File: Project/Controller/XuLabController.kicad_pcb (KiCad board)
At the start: 4 copper layers, 115 x 123 mm, 75 parts, among them J1 SWD Connector, J10 Servo, J11 Servo, J12 Thruster, J13 USB_B_Micro, J14 CAN, J15 I2C, J16 UART, J2 Conn_01x04, J3 1986660-2, J4 Servo, J5 Servo, J6 Servo, J7 Servo, J8 Servo, J9 Servo, Q2 PMOS, SW1 SW_Push, SW2 SW_SPDT, SW3 SW_SPDT, U1 STM32F446RCTx, U2 BMI088, U3 MMC5983MA, U4 AP63203WU, U5 TVS0500DRV, Y1 25 MHz

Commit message: Add initial layout
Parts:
- removed FL1: 0805USB-502MLC, Inductor_SMD:L_CommonModeChoke_Coilcraft_0805USB
- removed L1: 3.9uH, Inductor_SMD:L_Pulse_PA4334
- removed Q2: PMOS, XuLab:SOP-Advance-8
- removed TP2, TP3, TP4, TP5: TestPoint, TestPoint:TestPoint_Plated_Hole_D2.0mm
- added C26: 10uF, Capacitor_SMD:C_1206_3216Metric, F.Cu at (166.0, 86.0)
- added C27: 100nF, Capacitor_SMD:C_0603_1608Metric, B.Cu at (123.5, 64.5)
- added C28: 100nF, Capacitor_SMD:C_0603_1608Metric, B.Cu at (166.5, 64.5)
- added C29: 100nF, Capacitor_SMD:C_0603_1608Metric, B.Cu at (114.0, 70.0)
- added C30: 100nF, Capacitor_SMD:C_0603_1608Metric, B.Cu at (177.0, 70.0)
- added C31: 100nF, Capacitor_SMD:C_0603_1608Metric, B.Cu at (138.0, 64.5)
- added C32: 100nF, Capacitor_SMD:C_0603_1608Metric, B.Cu at (153.0, 64.5)
- added H1: MH, MountingHole:MountingHole_2.7mm_M2.5_Pad_Via, F.Cu at (121.0, 78.0)
- added H2: MH, MountingHole:MountingHole_2.7mm_M2.5_Pad_Via, F.Cu at (170.0, 78.0)
- added H3: MH, MountingHole:MountingHole_2.7mm_M2.5_Pad_Via, F.Cu at (121.0, 136.0)
- added H4: MH, MountingHole:MountingHole_2.7mm_M2.5_Pad_Via, F.Cu at (170.0, 136.0)
- added J17: UART2, Connector_JST:JST_GH_SM04B-GHS-TB_1x04-1MP_P1.25mm_Horizontal, F.Cu at (179.0, 70.0)
- added J18: SPI1, Connector_JST:JST_GH_SM06B-GHS-TB_1x06-1MP_P1.25mm_Horizontal, F.Cu at (138.0, 62.5)
- added J19: SPI2, Connector_JST:JST_GH_SM06B-GHS-TB_1x06-1MP_P1.25mm_Horizontal, F.Cu at (153.0, 62.5)
- added J20: Interrupt, Connector_Molex:Molex_KK-254_AE-6410-02A_1x02_P2.54mm_Vertical, F.Cu at (112.0, 93.5)
- added J21: Interrupt, Connector_Molex:Molex_KK-254_AE-6410-02A_1x02_P2.54mm_Vertical, F.Cu at (112.0, 86.5)
- added J22: Interrupt, Connector_Molex:Molex_KK-254_AE-6410-02A_1x02_P2.54mm_Vertical, F.Cu at (112.0, 79.5)
- added R12: 5k1, Resistor_SMD:R_0603_1608Metric, F.Cu at (154.0, 130.0)
- added R13: 5k1, Resistor_SMD:R_0603_1608Metric, F.Cu at (164.0, 130.0)
- added R14: 82k, Resistor_SMD:R_0603_1608Metric, B.Cu at (155.5, 101.5)
- added U6: USBLC6-2SC6, Package_TO_SOT_SMD:SOT-23-6, F.Cu at (159.0, 127.0)
- added U7: BMI088, Package_LGA:Bosch_LGA-16_4.5x3mm_P0.5mm_LayoutBorder7x1y_ClockwisePinNumbering, F.Cu at (154.0, 86.0)
- added U8: MMC5983MA, XuLab:MMC5983MA_MEM, F.Cu at (162.5, 86.0)
- added U9: MCP9700Ax-ETT, Package_TO_SOT_SMD:SOT-23, B.Cu at (129.0, 105.0)
- C1: value 4.7uF -> 1uF
- C10, C14, C22: footprint Capacitor_SMD:C_0402_1005Metric -> Capacitor_SMD:C_0603_1608Metric; moved to B.Cu
- C11, C12: value 22pF -> 100nF; footprint Capacitor_SMD:C_0402_1005Metric -> Capacitor_SMD:C_0603_1608Metric; moved to B.Cu
- C13: value 100nF -> 1uF; footprint Capacitor_SMD:C_0402_1005Metric -> Capacitor_SMD:C_0603_1608Metric; moved to B.Cu
- C15: value 1uF -> 100nF
- C16: value 10uF -> 27pF; footprint Capacitor_SMD:C_1206_3216Metric -> Capacitor_SMD:C_0603_1608Metric
- C17: value 100nF -> 27pF; footprint Capacitor_SMD:C_0402_1005Metric -> Capacitor_SMD:C_0603_1608Metric
- C18: value 100uF -> 100nF; footprint Capacitor_SMD:C_1210_3225Metric -> Capacitor_SMD:C_0603_1608Metric
- C19: value 10uF -> 2.2uF; footprint Capacitor_SMD:C_1206_3216Metric -> Capacitor_SMD:C_0603_1608Metric
- C2: value 100nF -> 10uF; footprint Capacitor_SMD:C_0402_1005Metric -> Capacitor_SMD:C_1206_3216Metric
- C20: value 1uF -> 100nF; moved to B.Cu
- C21: value 10uF -> 100nF; footprint Capacitor_SMD:C_1206_3216Metric -> Capacitor_SMD:C_0603_1608Metric; moved to B.Cu
- C23, C24: value 22uF -> 100nF; moved to B.Cu
- C25, C3, C6: value 100nF -> 1uF; footprint Capacitor_SMD:C_0402_1005Metric -> Capacitor_SMD:C_0603_1608Metric
- C4: value 100nF -> 470pF; footprint Capacitor_SMD:C_0402_1005Metric -> Capacitor_SMD:C_0603_1608Metric
- C5: value 100nF -> 2.2uF; footprint Capacitor_SMD:C_0402_1005Metric -> Capacitor_Tantalum_SMD:CP_EIA-3216-18_Kemet-A
- C7: value 1uF -> 4.7uF
- C8: footprint Capacitor_SMD:C_0402_1005Metric -> Capacitor_SMD:C_0603_1608Metric
- C9: value 2.2uF -> 100nF; moved to B.Cu
- D1: value LED -> 5V; footprint LED_SMD:LED_0603_1608Metric -> Diode_SMD:D_PowerDI-123
- D2: value RCLAMP0582B -> Red; footprint Package_TO_SOT_SMD:SOT-416 -> LED_SMD:LED_0603_1608Metric
- D3: value 12V -> Amber; footprint Diode_SMD:D_SOD-123 -> LED_SMD:LED_0603_1608Metric
- D4: value 7.5V -> Green; footprint Diode_SMD:D_SMB -> LED_SMD:LED_0603_1608Metric
- D5: value 3.3V -> Blue; footprint Diode_SMD:D_MicroSMP_KA -> LED_SMD:LED_0603_1608Metric
- FB1: moved to F.Cu
- J1: value SWD Connector -> Power; footprint Connector_IDC:IDC-Header_2x05_P2.54mm_Vertical -> Connector_JST:JST_GH_SM02B-GHS-TB_1x02-1MP_P1.25mm_Horizontal
- J10, J11, J5, J6, J7, J8, J9: footprint TerminalBlock_Phoenix:TerminalBlock_Phoenix_MKDS-1,5-3-5.08_1x03_P5.08mm_Horizontal -> Connector_JST:JST_VH_B2P-VH_1x02_P3.96mm_Vertical
- J12: value Thruster -> Servo; footprint Connector_JST:JST_VH_B3P-VH_1x03_P3.96mm_Vertical -> Connector_JST:JST_VH_B2P-VH_1x02_P3.96mm_Vertical
- J13: value USB_B_Micro -> Thruster; footprint Connector_USB:USB_Micro-B_Molex_47346-0001 -> Connector_JST:JST_VH_B2P-VH_1x02_P3.96mm_Vertical
- J14: value CAN -> I2C; footprint Connector_PinSocket_2.00mm:PinSocket_1x03_P2.00mm_Vertical -> Connector_JST:JST_GH_SM04B-GHS-TB_1x04-1MP_P1.25mm_Horizontal
- J15: footprint Connector_PinSocket_2.00mm:PinSocket_1x03_P2.00mm_Vertical -> Connector_JST:JST_GH_SM04B-GHS-TB_1x04-1MP_P1.25mm_Horizontal
- J16: value UART -> UART1; footprint Connector_PinSocket_2.00mm:PinSocket_1x03_P2.00mm_Vertical -> Connector_JST:JST_GH_SM04B-GHS-TB_1x04-1MP_P1.25mm_Horizontal
- J2: value Conn_01x04 -> SWD; footprint Connector_JST:JST_GH_SM04B-GHS-TB_1x04-1MP_P1.25mm_Horizontal -> Connector_PinHeader_2.54mm:PinHeader_2x03_P2.54mm_Vertical
- J3: value 1986660-2 -> USB_C_Receptacle_USB2.0_16P; footprint XuLab:CONN2_1986660-2_TEC -> Connector_USB:USB_C_Receptacle_GCT_USB4105-xx-A_16P_TopMnt_Horizontal
- J4: value Servo -> Bar30; footprint TerminalBlock_Phoenix:TerminalBlock_Phoenix_MKDS-1,5-3-5.08_1x03_P5.08mm_Horizontal -> Connector_JST:JST_GH_SM04B-GHS-TB_1x04-1MP_P1.25mm_Horizontal
- R1, R2: value 10k -> 47k; footprint Resistor_SMD:R_0402_1005Metric -> Resistor_SMD:R_0603_1608Metric
- R10: value 10k -> 100; moved to F.Cu
- R11: value 20k -> 33k
- R3: value 270 -> 330; footprint Resistor_SMD:R_0402_1005Metric -> Resistor_SMD:R_0603_1608Metric
- R4, R5: value 4k7 -> 10k; footprint Resistor_SMD:R_0402_1005Metric -> Resistor_SMD:R_0603_1608Metric
- R6, R7: value 22 -> 4k7; footprint Resistor_SMD:R_0402_1005Metric -> Resistor_SMD:R_0603_1608Metric
- R8: value 75 -> 330; footprint Resistor_SMD:R_0402_1005Metric -> Resistor_SMD:R_0603_1608Metric
- R9: value 100 -> 330; footprint Resistor_SMD:R_1206_3216Metric -> Resistor_SMD:R_0603_1608Metric
- SW1: value SW_Push -> SW_SPDT; footprint Button_Switch_SMD:SW_Push_1P1T_NO_E-Switch_TL3301NxxxxxG -> Button_Switch_SMD:Nidec_Copal_CAS-120A
- SW3: value SW_SPDT -> SW_Push; footprint Button_Switch_SMD:Nidec_Copal_CAS-120A -> Button_Switch_SMD:SW_Push_1P1T_NO_CK_KMR2
- TP1: value TestPoint -> Power; footprint TestPoint:TestPoint_Plated_Hole_D2.0mm -> TestPoint:TestPoint_2Pads_Pitch2.54mm_Drill0.8mm
- U1: value STM32F446RCTx -> LM66100DCK; footprint Package_QFP:LQFP-64_10x10mm_P0.5mm -> Package_TO_SOT_SMD:SOT-363_SC-70-6
- U2: value BMI088 -> MIC5219-3.3YM5; footprint Package_LGA:Bosch_LGA-16_4.5x3mm_P0.5mm_LayoutBorder7x1y_ClockwisePinNumbering -> Package_TO_SOT_SMD:SOT-23-5
- U3: value MMC5983MA -> LM66100DCK; footprint XuLab:MMC5983MA_MEM -> Package_TO_SOT_SMD:SOT-363_SC-70-6
- U4: value AP63203WU -> STM32F446RCTx; footprint Package_TO_SOT_SMD:TSOT-23-6 -> Package_QFP:LQFP-64_10x10mm_P0.5mm
- U5: value TVS0500DRV -> 24AA64-OT; footprint Package_SON:WSON-6-1EP_2x2mm_P0.65mm_EP1x1.6mm -> Package_TO_SOT_SMD:SOT-23-5
- Y1: value 25 MHz -> 8MHz; footprint Crystal:Crystal_SMD_Abracon_ABM8G-4Pin_3.2x2.5mm -> Crystal:Crystal_SMD_Abracon_ABM7-2Pin_6.0x3.5mm
- moved D2 101.6 mm to (129.5, 125.0), turned to 90 degrees
- moved J1 99.4 mm to (132.0, 137.0), turned to 0 degrees
- moved J8 87.2 mm to (114.0, 126.0), turned to -90 degrees
- moved R1 86.2 mm to (141.0, 134.0), turned to -90 degrees
- moved R2 83.7 mm to (150.0, 134.0), turned to 90 degrees
- moved J4 79.9 mm to (179.0, 81.0), turned to 90 degrees
- moved SW2 76.7 mm to (162.5, 103.5), turned to 0 degrees
- moved U3 71.5 mm to (148.0, 138.0), turned to 180 degrees
- moved J12 68.5 mm to (177.0, 130.0)
- moved U5 68.3 mm to (138.5, 86.0), turned to 90 degrees
- moved U2 64.6 mm to (145.5, 127.5), turned to 90 degrees
- moved C1 61.7 mm to (139.0, 134.0), turned to -90 degrees
- moved C17 60.1 mm to (128.0, 100.5), turned to 90 degrees
- moved C2 59.5 mm to (145.5, 134.0), turned to 0 degrees
- moved C3 59.3 mm to (145.5, 131.5), turned to 0 degrees
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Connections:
- C1 pad 1: +3.3V -> Net-(D1-K)
- C10 pad 1: /MCU A/NRST -> +3.3V
- C11 pad 1: /MCU A/RCC_IN -> +3.3V
- C12 pad 1: Net-(C12-Pad1) -> +3.3V
- C13 pad 1: +3.3V -> +3.3VA
- C14 pad 1: +3.3V -> +3.3VA
- C15 pad 1: +3.3V -> /Microcontroller/NRST
- C16 pad 1: Net-(U3-CAP) -> /Microcontroller/RCC_IN
- C17 pad 1: +3.3V -> /Microcontroller/RCC_OUT
- C18 pad 1: +7.4V -> +3.3V
- C19 pad 1: +7.4V -> Net-(U4-VCAP_1)
- C2 pad 1: +3.3V -> Net-(U1-VOUT)
- C20 pad 1: +7.4V -> /Microcontroller/USB_VBUS
- C21 pad 1: +7.4V -> +3.3V
- C22 pad 1: Net-(U4-BST) -> +3.3V
- C22 pad 2: Net-(U4-SW) -> GND
- C25 pad 1: /MCU A/USB_VBUS -> +3.3V
- C3 pad 1: +3.3V -> Net-(U1-VOUT)
- C4 pad 1: +3.3V -> Net-(U2-BP)
- C6 pad 1: +3.3V -> /USB_Power
- C7 pad 1: +3.3VA -> +3.3V
- C8 pad 1: +3.3VA -> +3.3V
- C9 pad 1: Net-(U1-VCAP_1) -> +3.3V
- D1 pad 2: /MCU A/LED_OUT -> GND
- D2 pad 1: /MCU A/USB_D_I- -> Net-(D2-K)
- D2 pad 2: /MCU A/USB_D_I+ -> +3.3V
- D3 pad 1: +7.4V -> Net-(D3-K)
- D3 pad 2: Net-(D3-A) -> /Microcontroller/LED_OUT1
- D4 pad 1: +7.4V -> Net-(D4-K)
- D4 pad 2: GND -> /Microcontroller/LED_OUT2
- D5 pad 1: +3.3V -> Net-(D5-K)
- D5 pad 2: GND -> /Microcontroller/LED_OUT3
- J1 pad 1: +3.3V -> Net-(D1-K)
- J1 pad 2: /MCU A/SW_DIO -> GND
- J10 pad 1: GND -> /PWM_6
- J10 pad 2: +7.4V -> GND
- J11 pad 1: GND -> /PWM_7
- J11 pad 2: +7.4V -> GND
- J12 pad 1: GND -> /PWM_8
- J12 pad 2: +3.3V -> GND
- J13 pad 1: /MCU A/USB_VBUS_I -> /PWM_9
- J13 pad 2: /MCU A/USB_D_I- -> GND
- J14 pad 1: /CAN1_TX -> +3.3V
- J14 pad 2: /CAN1_RX -> /I2C1_SCL
- J14 pad 3: GND -> /I2C1_SDA
- J15 pad 1: /I2C1_SDA -> +3.3V
- J15 pad 3: GND -> /I2C1_SDA
- J16 pad 1: /UART_RX -> +3.3V
- J16 pad 2: /UART_TX -> /UART1_TX
- J16 pad 3: GND -> /UART1_RX
- J2 pad 2: /I2C1_SCL -> /Microcontroller/SW_DIO
- J2 pad 3: /I2C1_SDA -> /Microcontroller/NRST
- J2 pad 4: GND -> /Microcontroller/SW_CLK
- J4 pad 1: /PWM_1 -> +3.3V
- J4 pad 2: +7.4V -> /I2C1_SCL
- J4 pad 3: GND -> /I2C1_SDA
- J5 pad 1: /PWM_2 -> /PWM_1
- J5 pad 2: +7.4V -> GND
- J6 pad 1: /PWM_3 -> /PWM_2
- J6 pad 2: +7.4V -> GND
- J7 pad 1: /PWM_4 -> /PWM_3
- J7 pad 2: +7.4V -> GND
- J8 pad 1: GND -> /PWM_4
- J8 pad 2: +7.4V -> GND
- J9 pad 1: GND -> /PWM_5
- J9 pad 2: +7.4V -> GND
- R1 pad 1: Net-(SW2-B) -> Net-(D1-K)
- R1 pad 2: /MCU A/BOOT0 -> /Power/Status
- R10 pad 1: /MCU A/USB_VBUS_I -> Net-(D5-K)
- R10 pad 2: /MCU A/USB_VBUS -> GND
- R11 pad 1: /MCU A/USB_VBUS -> /USB_Power
- R11 pad 2: GND -> /Microcontroller/USB_VBUS
- R2 pad 1: Net-(SW3-B) -> Net-(U1-~{CE})
- R2 pad 2: /MCU A/BOOT1 -> /USB_Power
- R3 pad 1: /MCU A/RCC_OUT -> Net-(D2-K)
- R3 pad 2: Net-(C12-Pad1) -> GND
- R4 pad 1: +3.3V -> Net-(SW1-B)
- R4 pad 2: /I2C1_SCL -> /Microcontroller/BOOT0
- R5 pad 1: +3.3V -> Net-(SW2-B)
- R5 pad 2: /I2C1_SDA -> /Microcontroller/BOOT1
- R6 pad 1: /MCU A/USB_D+ -> +3.3V
- R6 pad 2: /MCU A/USB_D_M+ -> /I2C1_SCL
- R7 pad 1: /MCU A/USB_D- -> +3.3V
- R7 pad 2: /MCU A/USB_D_M- -> /I2C1_SDA
- R8 pad 1: Net-(D1-K) -> Net-(D3-K)
- R9 pad 1: Net-(D3-A) -> Net-(D4-K)
- SW1 pad 1: /MCU A/NRST -> GND
- SW1 pad 2: GND -> Net-(SW1-B)
- SW3 pad 1: GND -> /Microcontroller/NRST
- SW3 pad 2: Net-(SW3-B) -> GND
- TP1 pad 1: +7.4V -> +3.3V
- U1 pad 1: +3.3V -> Net-(D1-K)
- U1 pad 2: unconnected-(U1-PC13-Pad2) -> GND
- U1 pad 3: unconnected-(U1-PC14-Pad3) -> Net-(U1-~{CE})
- U1 pad 5: /MCU A/RCC_IN -> /Power/Status
- U1 pad 6: /MCU A/RCC_OUT -> Net-(U1-VOUT)
- U2 pad 1: /Attitude and Heading Module/ACCL_INT2 -> Net-(U1-VOUT)
- U2 pad 3: +3.3V -> Net-(U1-VOUT)
- U2 pad 4: GND -> Net-(U2-BP)
- U2 pad 5: /SPI1_CS2 -> +3.3V
- U3 pad 1: /SPI1_SCK -> /USB_Power
- U3 pad 2: +3.3V -> GND
- U3 pad 3: unconnected-(U3-NC-Pad3) -> /Power/Status
- U3 pad 4: /SPI1_CS3 -> unconnected-(U3-NC-Pad4)
- U3 pad 5: /SPI1_MISO -> unconnected-(U3-ST-Pad5)
- U3 pad 6: unconnected-(U3-NC-Pad6) -> Net-(U1-VOUT)
- U4 pad 2: +7.4V -> /GPIO_EXTI13
- U4 pad 3: +7.4V -> /GPIO_EXTI14
- U4 pad 4: GND -> /GPIO_EXTI15
- U4 pad 5: Net-(U4-SW) -> /Microcontroller/RCC_IN
- U4 pad 6: Net-(U4-BST) -> /Microcontroller/RCC_OUT
- U5 pad 1: GND -> /I2C1_SCL
- U5 pad 3: GND -> /I2C1_SDA
- U5 pad 4: /MCU A/USB_VBUS_I -> +3.3V
- U5 pad 5: /MCU A/USB_VBUS_I -> GND
- Y1 pad 1: /MCU A/RCC_IN -> /Microcontroller/RCC_IN
- Y1 pad 2: GND -> /Microcontroller/RCC_OUT
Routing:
- net GND: track 127.6 -> 0.00 mm, vias 65 -> 0
- net /MCU A/NRST: track 109.9 -> 0.00 mm, vias 1 -> 0
- net /I2C1_SDA: track 82.6 -> 0.00 mm, vias 2 -> 0
- net /I2C1_SCL: track 82.0 -> 0.00 mm, vias 2 -> 0
- net /PWM_5: track 77.9 -> 0.00 mm
- net /PWM_4: track 70.1 -> 0.00 mm
- net /PWM_9: track 63.6 -> 0.00 mm
- net /MCU A/BOOT1: track 63.2 -> 0.00 mm, vias 2 -> 0
- net /PWM_6: track 62.8 -> 0.00 mm
- net /CAN1_TX: track 62.4 -> 0.00 mm
- net /PWM_8: track 62.2 -> 0.00 mm
- net /CAN1_RX: track 60.6 -> 0.00 mm
- net /MCU A/USB_D_I-: track 57.7 -> 0.00 mm
- net +3.3V: track 57.0 -> 0.00 mm, vias 19 -> 0
- net /MCU A/USB_D_I+: track 57.0 -> 0.00 mm
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- removed copper zone on B.Cu, net +3.3V
- removed copper zone on F.Cu, net +3.3V
- removed copper zone on In2.Cu, net +3.3V
- removed copper zone on B.Cu, net +7.4V
- removed copper zone on F.Cu, net +7.4V
- removed copper zone on In2.Cu, net +7.4V
- removed copper zone on F.Cu, net GND
- removed copper zone on In1.Cu, net GND
- removed copper zone on B.Cu, net Net-(Q2-D)
- removed copper zone on F.Cu, net Net-(Q2-D)
- removed copper zone on F.Cu, net Net-(U4-SW)
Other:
- board size 115 x 123 mm -> 75 x 81 mm
- board text removed: "+IN"
- board text removed: "+X"
- board text removed: "+Y"
- board text removed: "+Z"
- board text removed: "-IN"
- board text removed: "3V3"
- board text removed: "7V4"
- board text removed: "BOOT0"
- board text removed: "BOOT1"
- board text removed: "CAN"
- board text removed: "CLK"
- board text removed: "DIO"
- board text removed: "GND"
- board text removed: "I2C"
- board text removed: "LED Output"
- board text removed: "PWM"
- board text removed: "RST"
- board text removed: "RX"
- board text removed: "Reset"
- board text removed: "SCL"
- board text removed: "SDA"
- board text removed: "SWO"
- board text removed: "Serial Wire Debug"
- board text removed: "TX"
- board text removed: "UART"
- board text removed: "X"
- board text removed: "Xu Lab Eval Board Rev. A - 12/25"

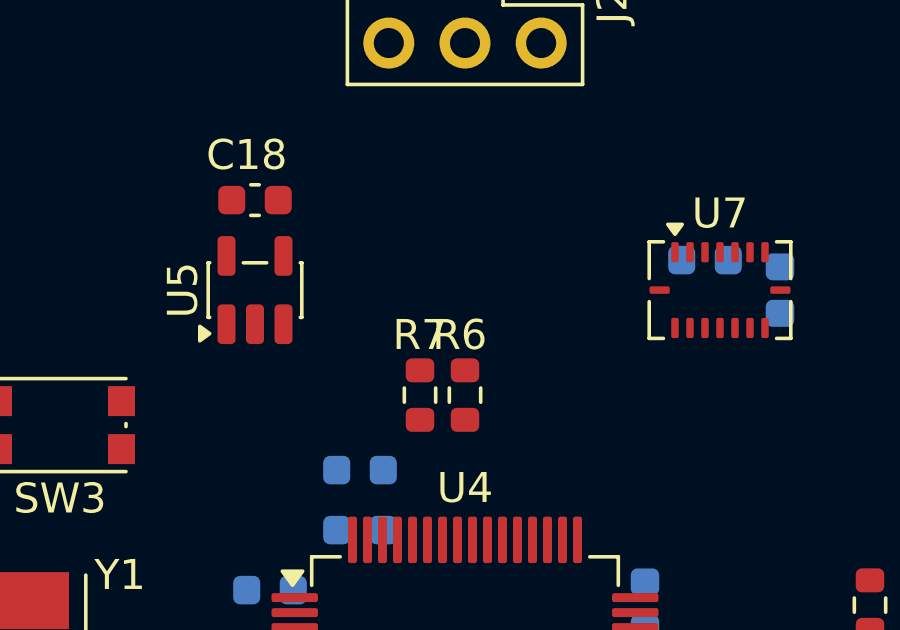
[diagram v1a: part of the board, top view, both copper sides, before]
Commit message: Add SHTC3 humidity sensor
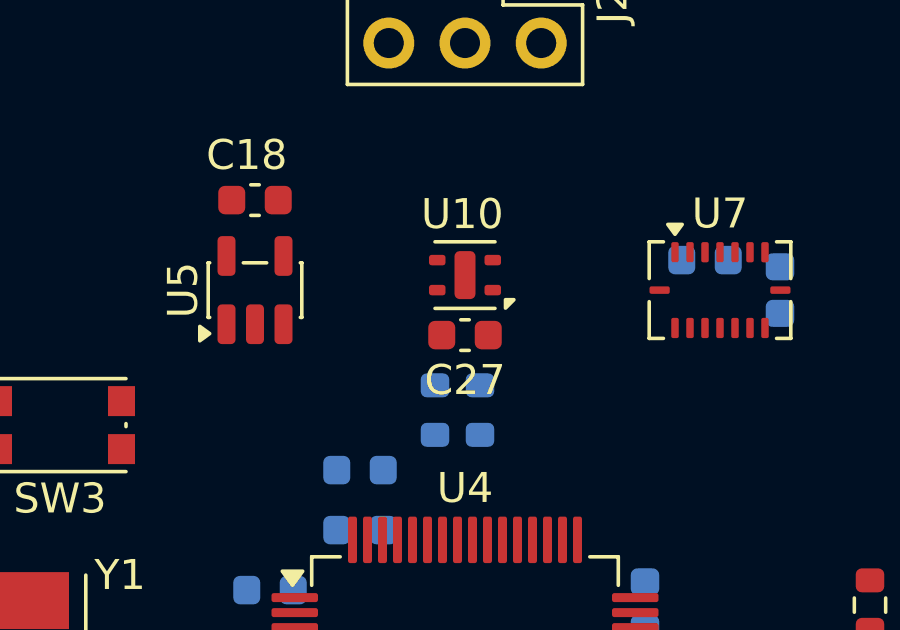
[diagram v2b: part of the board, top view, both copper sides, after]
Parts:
- added C27: 100nF, Capacitor_SMD:C_0603_1608Metric, F.Cu at (145.5, 87.5)
- added U10: SHTC3, Sensor_Humidity:Sensirion_DFN-4-1EP_2x2mm_P1mm_EP0.7x1.6mm, F.Cu at (145.5, 85.5)
- R6, R7: moved to B.Cu
- moved R6 0.71 mm to (146.0, 90.0)
- moved R7 0.71 mm to (144.5, 90.0)
- renumbered C27 to C28, C28 to C29, C29 to C30, C30 to C31, C31 to C32, C32 to C33

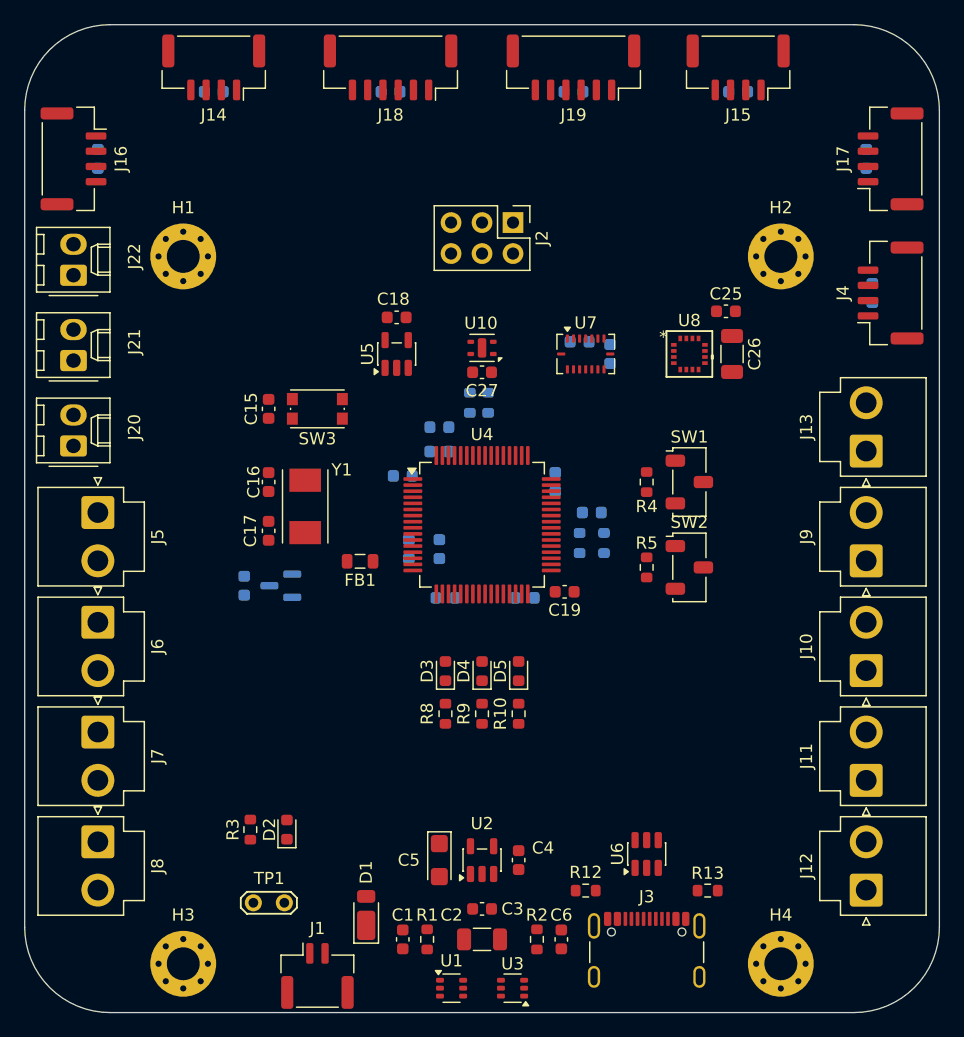
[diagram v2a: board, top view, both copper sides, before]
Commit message: Add trace routing
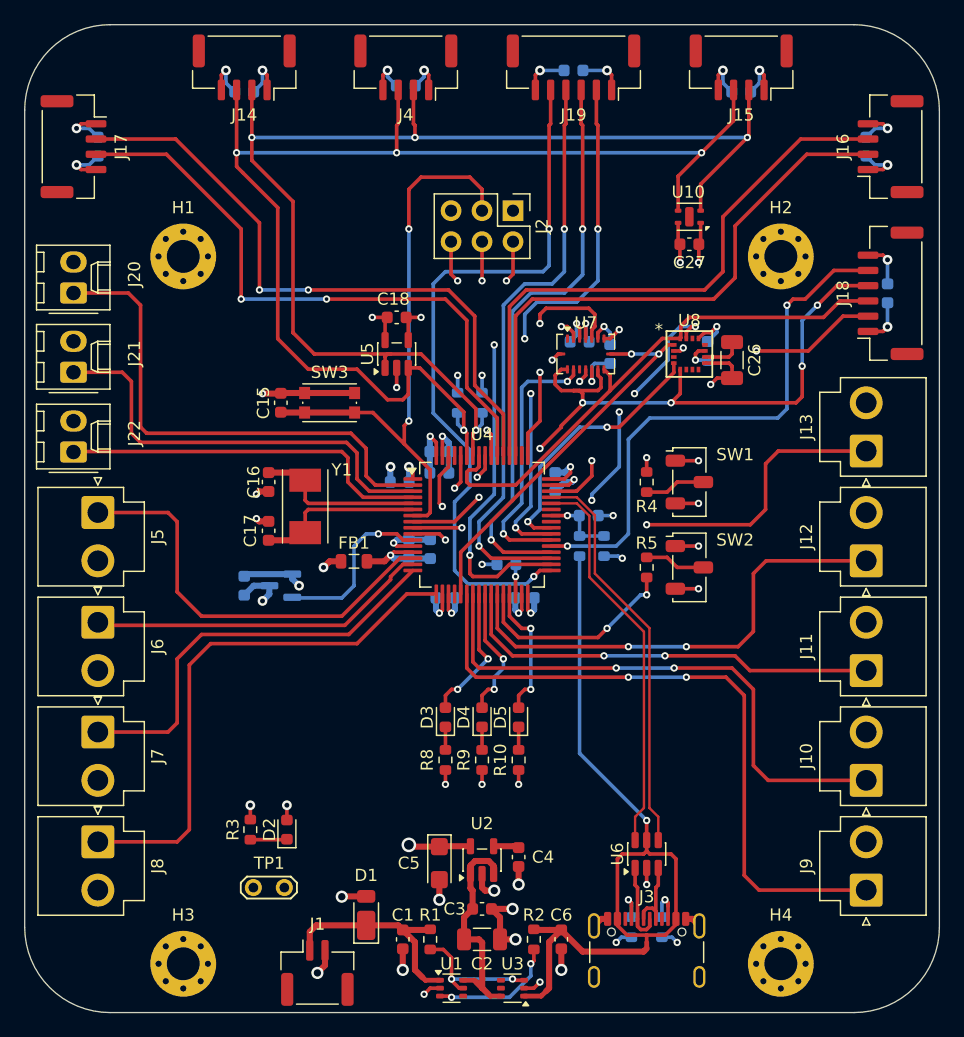
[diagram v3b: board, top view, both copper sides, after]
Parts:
- C19, C25, R12, R13: moved to B.Cu
- moved J16 67.0 mm to (179.0, 69.0), turned to 90 degrees
- moved J17 67.0 mm to (112.0, 69.0), turned to -90 degrees
- moved C30 63.0 mm to (177.0, 69.0), turned to 90 degrees
- moved C31 63.0 mm to (114.0, 69.0), turned to -90 degrees
- moved J18 45.0 mm to (179.0, 81.0), turned to 90 degrees
- moved C32 44.0 mm to (178.8, 81.0), turned to 90 degrees
- moved J4 43.8 mm to (139.2, 62.5), turned to 180 degrees
- moved C23 41.9 mm to (139.2, 64.0), turned to 180 degrees
- moved J12 27.0 mm to (177.0, 103.0)
- moved J9 27.0 mm to (177.0, 130.0)
- moved U10 20.1 mm to (162.5, 74.8)
- moved C27 20.0 mm to (162.5, 77.0)
- moved J22 14.5 mm to (112.0, 94.0)
- moved J20 12.5 mm to (112.0, 81.0)
- moved J10 9.00 mm to (177.0, 121.0)
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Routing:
- net GND: track 0.00 -> 128.0 mm, vias 0 -> 49
- net /I2C1_SDA: track 0.00 -> 103.4 mm, vias 0 -> 4
- net /I2C1_SCL: track 0.00 -> 102.0 mm, vias 0 -> 4
- net +3.3V: track 0.00 -> 80.5 mm, vias 0 -> 26
- net /USB_Power: track 0.00 -> 66.9 mm, vias 0 -> 1
- net /SPI2_NSS: track 0.00 -> 58.7 mm, vias 0 -> 2
- net /SPI1_MISO: track 0.00 -> 57.1 mm, vias 0 -> 6
- net /PWM_5: track 0.00 -> 55.0 mm, vias 0 -> 2
- net /SPI2_SCK: track 0.00 -> 54.3 mm, vias 0 -> 4
- net /UART2_TX: track 0.00 -> 52.7 mm, vias 0 -> 2
- net /UART2_RX: track 0.00 -> 51.5 mm, vias 0 -> 2
- net /SPI1_SCK: track 0.00 -> 50.4 mm, vias 0 -> 3
- net /UART1_RX: track 0.00 -> 49.9 mm
- net /Microcontroller/NRST: track 0.00 -> 48.8 mm, vias 0 -> 2
- net /UART1_TX: track 0.00 -> 48.3 mm
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- added copper zone on In2.Cu, net +3.3V
- added copper zone on In1.Cu, net GND

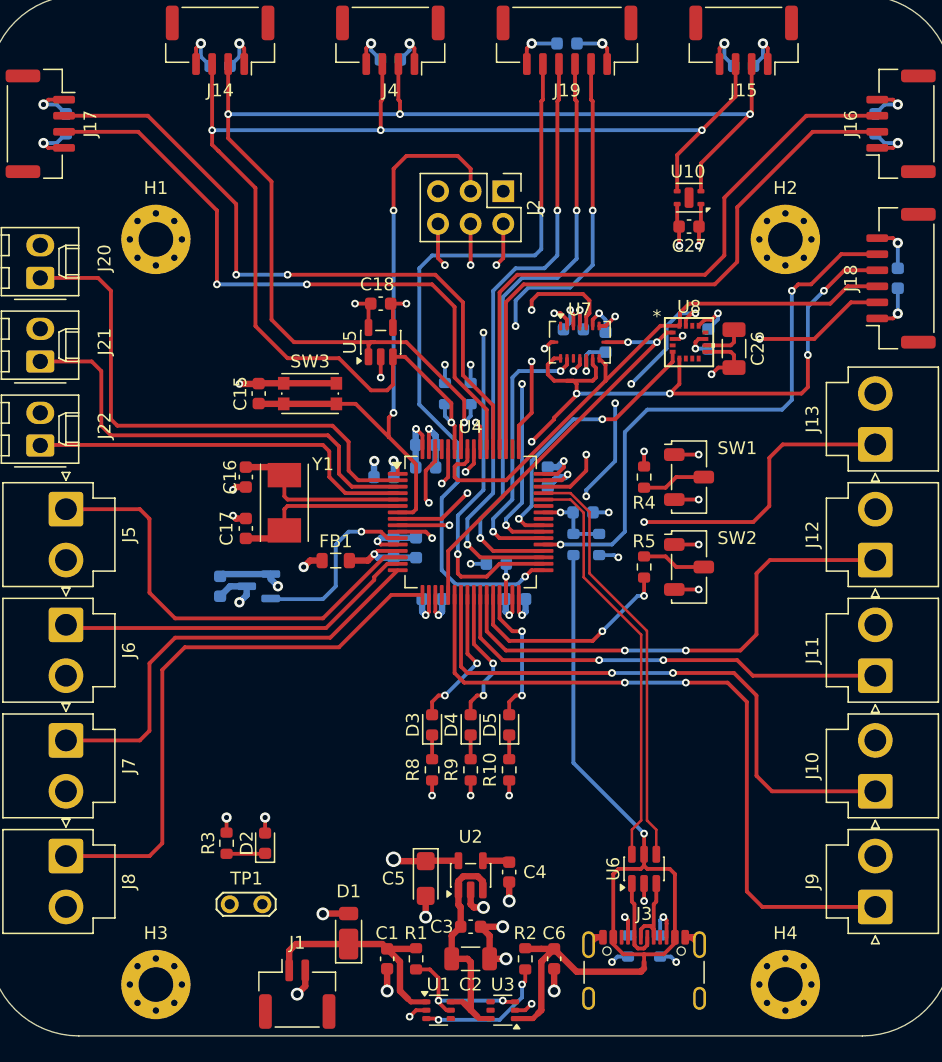
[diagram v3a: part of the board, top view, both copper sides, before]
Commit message: Move part references to fabrication layers
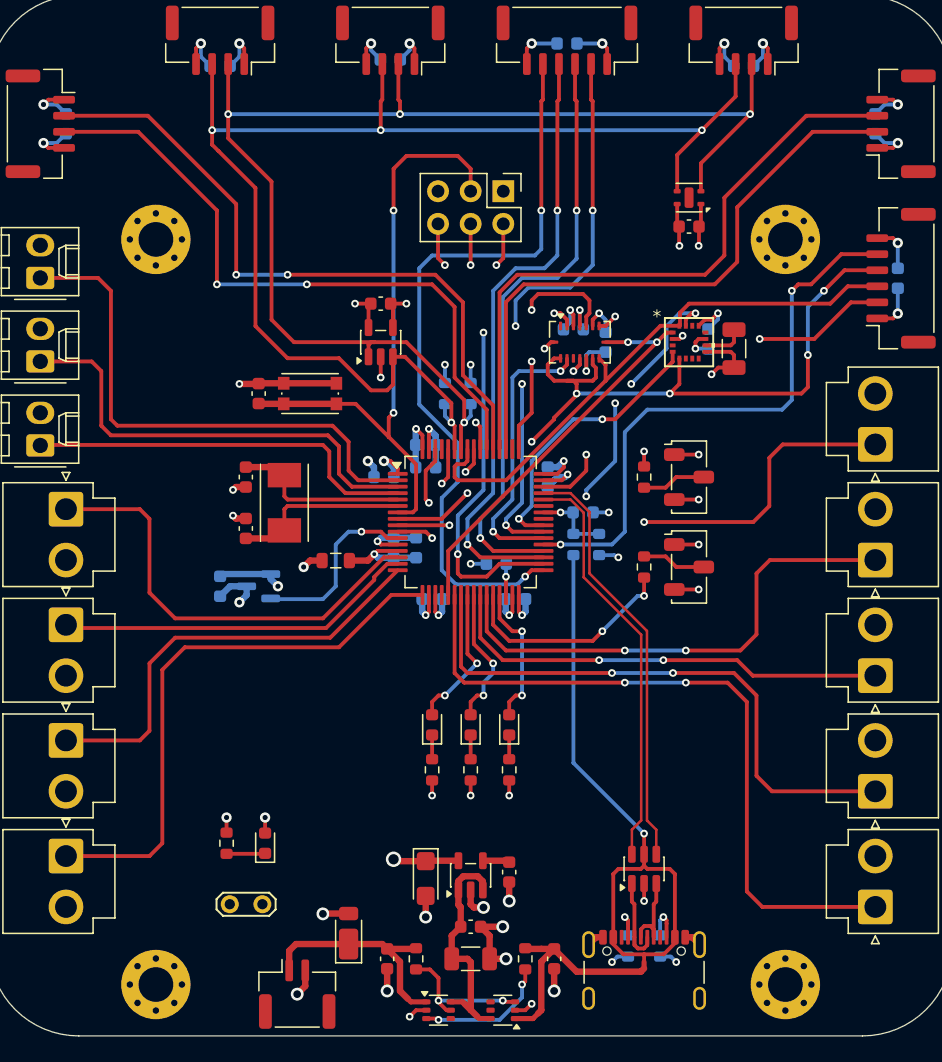
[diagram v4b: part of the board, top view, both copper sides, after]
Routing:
- net +3.3V: track 80.5 -> 81.6 mm

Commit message: Add silkscreen labeling
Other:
- board text added: "0"
- board text added: "1"
- board text added: "3.3 V"
- board text added: "3V3"
- board text added: "BOOT0"
- board text added: "BOOT1"
- board text added: "CLK"
- board text added: "CS"
- board text added: "D1"
- board text added: "D2"
- board text added: "D3"
- board text added: "DIO"
- board text added: "Designed By: Owen Allison"
- board text added: "EXTI"
- board text added: "EXTI13"
- board text added: "EXTI14"
- board text added: "EXTI15"
- board text added: "GND"
- board text added: "I2C"
- board text added: "IMU"
- board text added: "MAG"
- board text added: "MISO"
- board text added: "MOSI"
- board text added: "PWM"
- board text added: "PWM1"
- board text added: "PWM2"
- board text added: "PWM3"
- board text added: "PWM4"
- board text added: "PWM5"
- board text added: "PWM6"
- board text added: "PWM7"
- board text added: "PWM8"
- board text added: "PWM9"
- board text added: "RESET"
- board text added: "RST"
- board text added: "RX"
- board text added: "SCK"
- board text added: "SCL"
- board text added: "SDA"
- board text added: "SERIAL WIRE"
- board text added: "SPI1"
- board text added: "SPI2"
- board text added: "SWO"
- board text added: "TX"
- board text added: "Team 29: Owen Allison Jose Cabrera Sean Curry Alex Hansen Anthony Javier Topher Prokopius Ilsa Runge Leon Steinbach Carter Winkleman"
- board text added: "UART1"
- board text added: "UART2"
- board text added: "X+"
- board text added: "Y+"
